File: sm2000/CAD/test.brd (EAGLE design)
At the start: 160 x 100 mm, 30 parts, among them Q1 BRF92, Q2 BFQ19, Q3 BFQ19, X1 BU-SMA-G, X2 BU-SMA-G

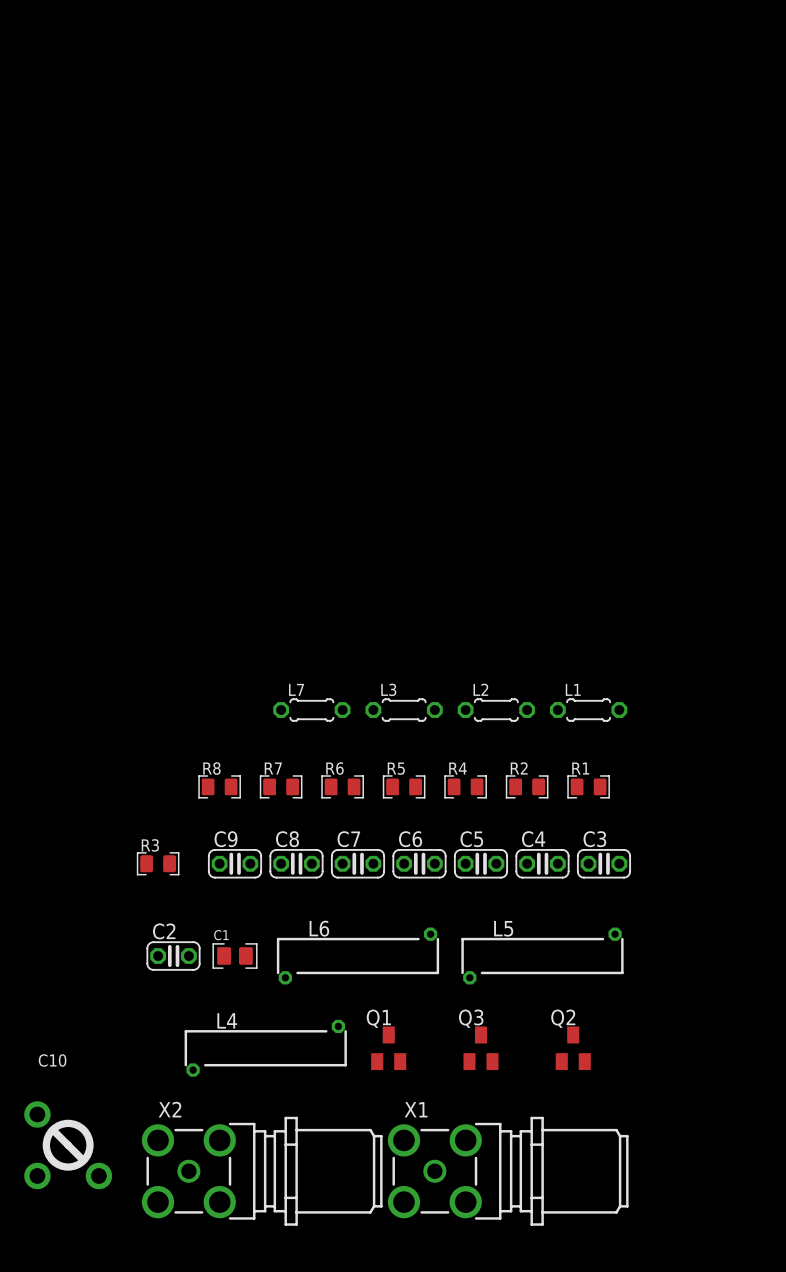
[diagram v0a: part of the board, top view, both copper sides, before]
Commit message: Update schematic & PCB RGB
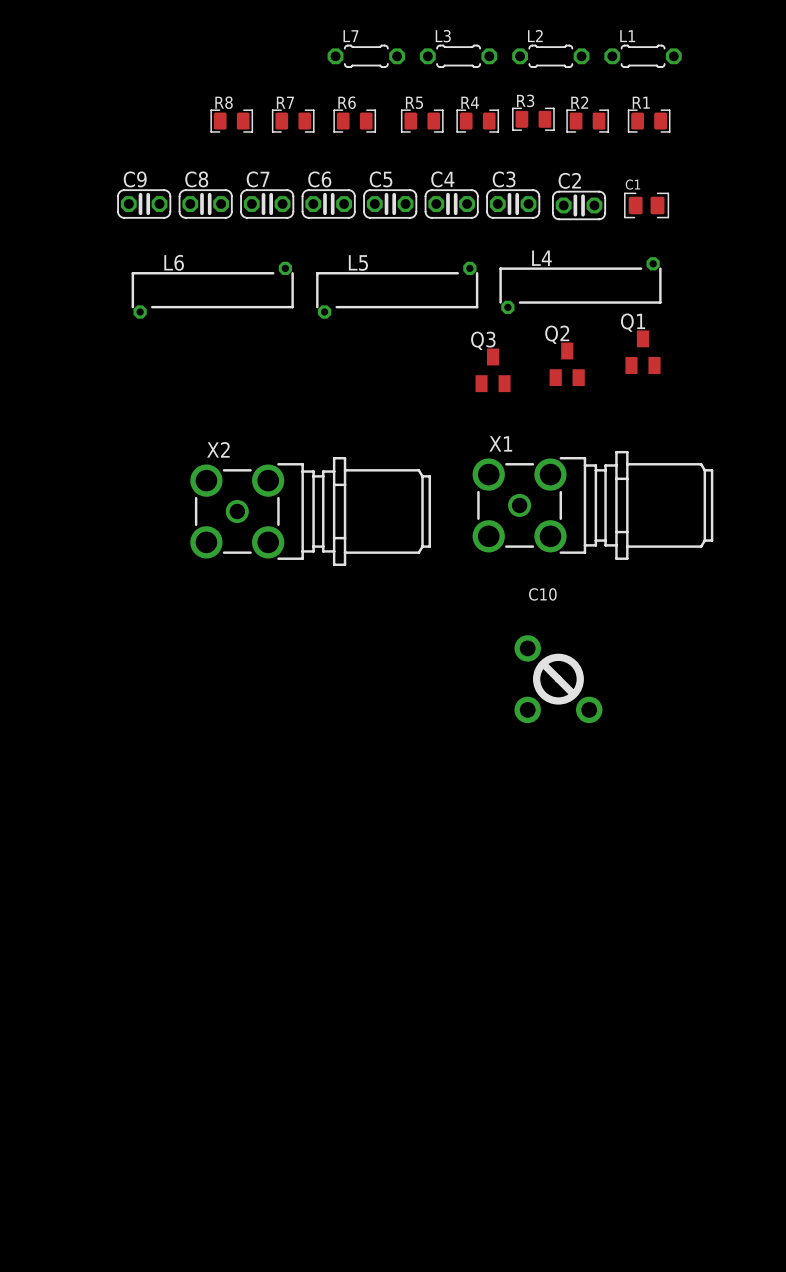
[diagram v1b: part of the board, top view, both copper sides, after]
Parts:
- moved C1 70.7 mm to (-11.7, 86.1)
- moved C2 70.5 mm to (-17.3, 86.1)
- moved R3 68.9 mm to (-21.1, 93.2)
- moved L4 68.2 mm to (-17.2, 79.5)
- moved Q1 61.2 mm to (-12.0, 74.0)
- moved Q2 56.5 mm to (-18.3, 73.0)
- moved L5 56.3 mm to (-32.3, 79.1)
- moved L6 56.3 mm to (-47.6, 79.1)
- moved Q3 56.0 mm to (-24.4, 72.5)
- moved C10 55.9 mm to (-19.0, 47.0)
- moved X1 55.4 mm to (-22.2, 61.4)
- moved R1 55.2 mm to (-11.5, 93.1)
- moved R2 55.2 mm to (-16.6, 93.1)
- moved R5 55.0 mm to (-30.2, 93.1)
- moved C3 55.0 mm to (-22.7, 86.2)
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
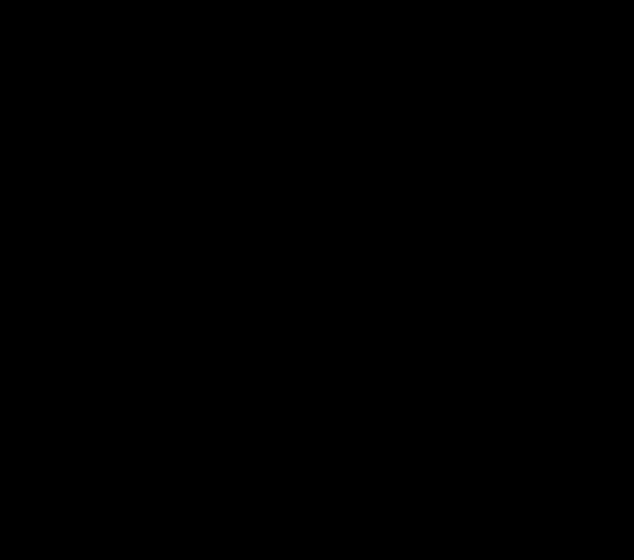
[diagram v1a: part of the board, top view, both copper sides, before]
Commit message: Add rowetel.lbr with new SM2000 components. RGB
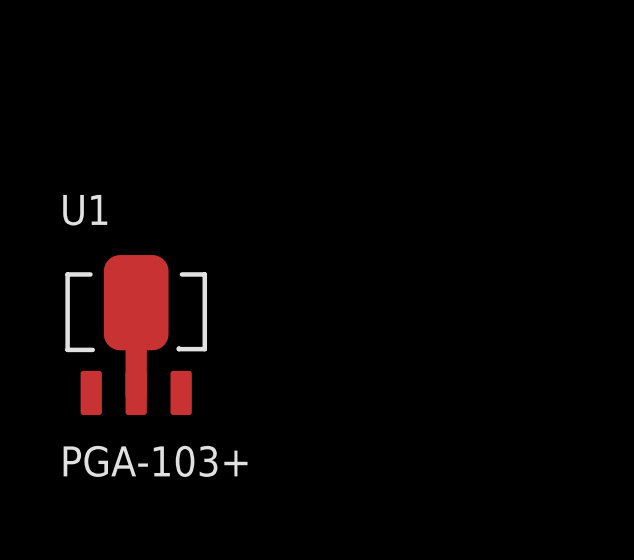
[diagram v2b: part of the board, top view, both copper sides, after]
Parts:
- added U1: PGA-103+, _RoweTel:DF782
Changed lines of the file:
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@@
 <element name="C9" library="rcl" package="C025-024X044" value="22p" x="-53.22" y="86.25"/>
 <element name="C10" library="_RoweTel" package="TRIMCAP_VAR_2222_V" value="TRIMCAP_VAR_2222_V" x="-19" y="47"/>
+<element name="U1" library="_RoweTel" package="DF782" value="PGA-103+" x="-59" y="5.5"/>
 </elements>
 <signals>
